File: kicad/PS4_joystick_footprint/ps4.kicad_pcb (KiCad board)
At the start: 2 copper layers, 20 x 28.5 mm, 2 parts, among them J1 Joystick, U1 COM-09032

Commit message: update pcb and documentation
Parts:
- added SW1: SW_Push, Button_Switch_SMD:SW_SPST_B3S-1000, F.Cu at (119.5, 140.5)
- added SW2: SW_Push, Button_Switch_SMD:SW_SPST_B3S-1000, F.Cu at (130.0, 151.0)
- added SW3: SW_Push, Button_Switch_SMD:SW_SPST_B3S-1000, F.Cu at (140.5, 140.5)
- added SW4: SW_Push, Button_Switch_SMD:SW_SPST_B3S-1000, F.Cu at (130.0, 130.0)
- J1: value Joystick -> Conn_01x11_Pin; footprint Connector_PinHeader_2.54mm:PinHeader_1x07_P2.54mm_Vertical -> Connector_PinHeader_2.54mm:PinHeader_1x11_P2.54mm_Vertical
- moved J1 23.9 mm to (91.9, 153.0), turned to 180 degrees
- moved U1 3.33 mm to (104.6, 144.0)
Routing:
- net /L2: track 0.00 -> 78.9 mm
- net /R2: track 0.00 -> 64.1 mm
- net /L1: track 0.00 -> 63.2 mm
- net /R1: track 0.00 -> 61.7 mm
- net /Switch: track 6.15 -> 18.4 mm
- net /R_black: track 17.3 -> 9.50 mm
- net /R_orange: track 24.4 -> 18.5 mm
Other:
- board size 20 x 28.5 mm -> 55.5 x 30 mm

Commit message: update joystick pcb
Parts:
- SW1: value SW_Push -> X
- SW2: value SW_Push -> A
- SW3: value SW_Push -> B
- SW4: value SW_Push -> Y
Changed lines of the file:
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@@
 		(tags "Tactile Switch")
 		(property "Reference" "SW4"
-			(at 0 4.3 180)
+			(at 0 0 180)
 			(layer "F.SilkS")
 			(effects
@@
 			)
 		)
-		(property "Value" "SW_Push"
+		(property "Value" "Y"
 			(at 0 4.5 0)
-			(layer "F.Fab")
-			(effects
-				(font
-					(size 1 1)
+			(layer "F.SilkS")
+			(effects
+				(font
+					(size 1.5 1.5)
 					(thickness 0.15)
 				)
@@
 		(tags "Tactile Switch")
 		(property "Reference" "SW1"
-			(at 0 5.1 180)
+			(at 0 0.04 180)
 			(layer "F.SilkS")
 			(effects
@@
 			)
 		)
-		(property "Value" "SW_Push"
-			(at 0 4.5 90)
-			(layer "F.Fab")
-			(effects
-				(font
-					(size 1 1)
+		(property "Value" "X"
+			(at 0 4.5 180)
+			(layer "F.SilkS")
+			(effects
+				(font
+					(size 1.5 1.5)
 					(thickness 0.15)
 				)
@@
 		(tags "Tactile Switch")
 		(property "Reference" "SW3"
-			(at 0 5.1 0)
+			(at -0.1 0 0)
 			(layer "F.SilkS")
 			(effects
@@
 			)
 		)
-		(property "Value" "SW_Push"
-			(at 0 4.5 90)
-			(layer "F.Fab")
-			(effects
-				(font
-					(size 1 1)
+		(property "Value" "B"
+			(at 0 4.5 180)
+			(layer "F.SilkS")
+			(effects
+				(font
+					(size 1.5 1.5)
 					(thickness 0.15)
 				)
@@
 		(tags "Tactile Switch")
 		(property "Reference" "SW2"
-			(at 0 -4.2 0)
+			(at 0 0 0)
 			(layer "F.SilkS")
 			(effects
@@
 			)
 		)
-		(property "Value" "SW_Push"
-			(at 0 4.5 0)
-			(layer "F.Fab")
-			(effects
-				(font
-					(size 1 1)
+		(property "Value" "A"
+			(at 0 -4.5 0)
+			(layer "F.SilkS")
+			(effects
+				(font
+					(size 1.5 1.5)
 					(thickness 0.15)
 				)
@@
 		)
 		(fp_text user "${REFERENCE}"
-			(at 0 -4.5 0)
-			(layer "F.Fab")
-			(effects
+			(at 0 4.5 0)
+			(layer "F.Fab")
+			(effects

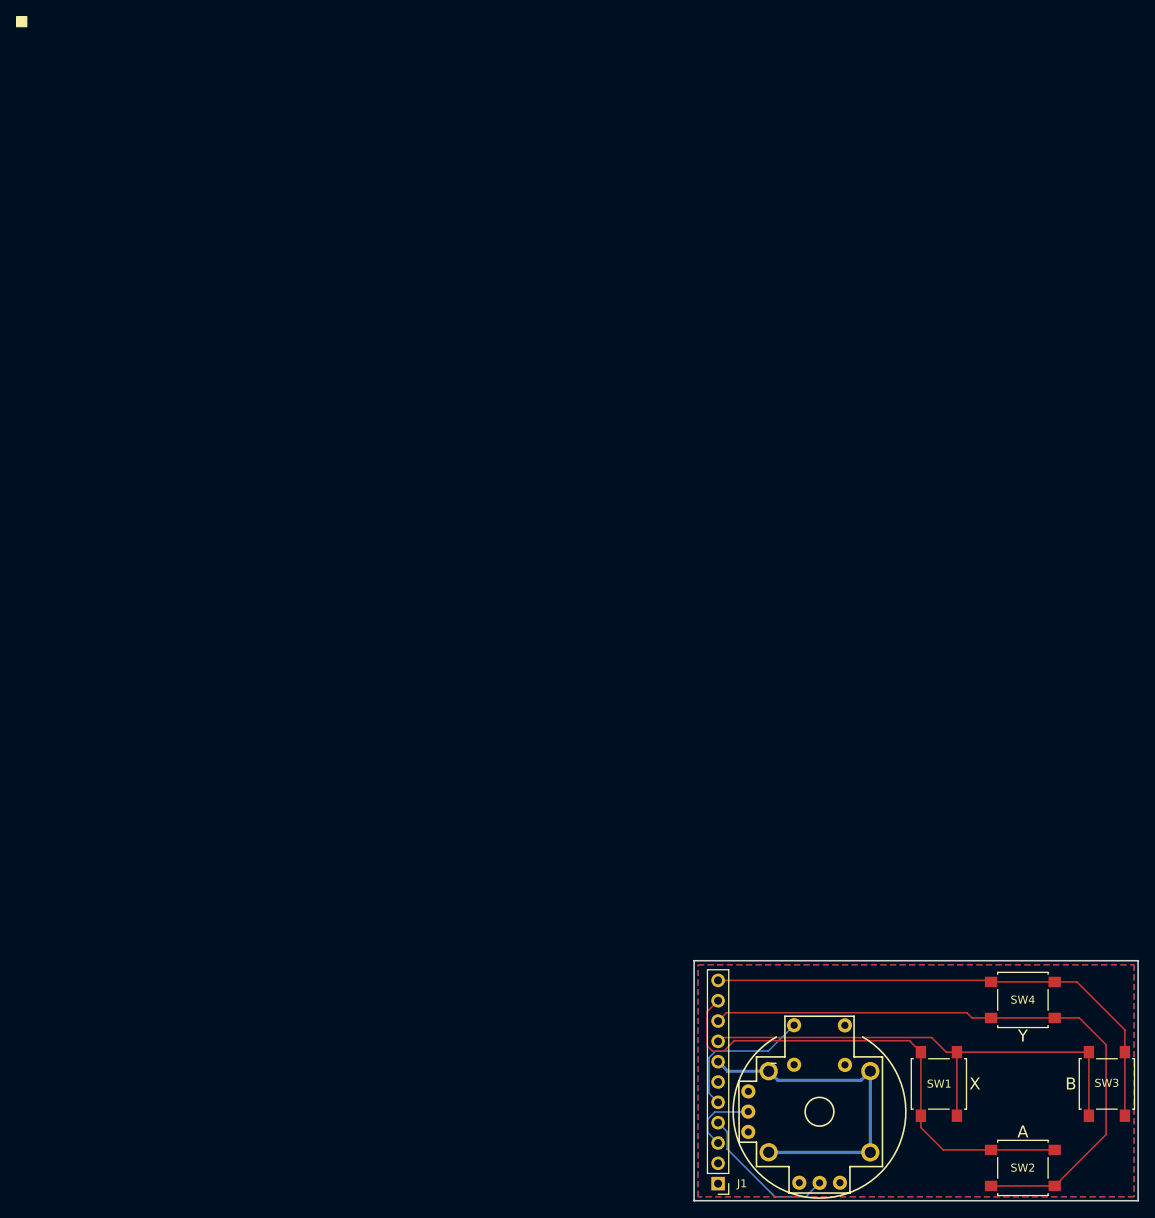
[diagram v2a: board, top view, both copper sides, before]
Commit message: add little-scale/PS4_joystick_footprint next to the footprint
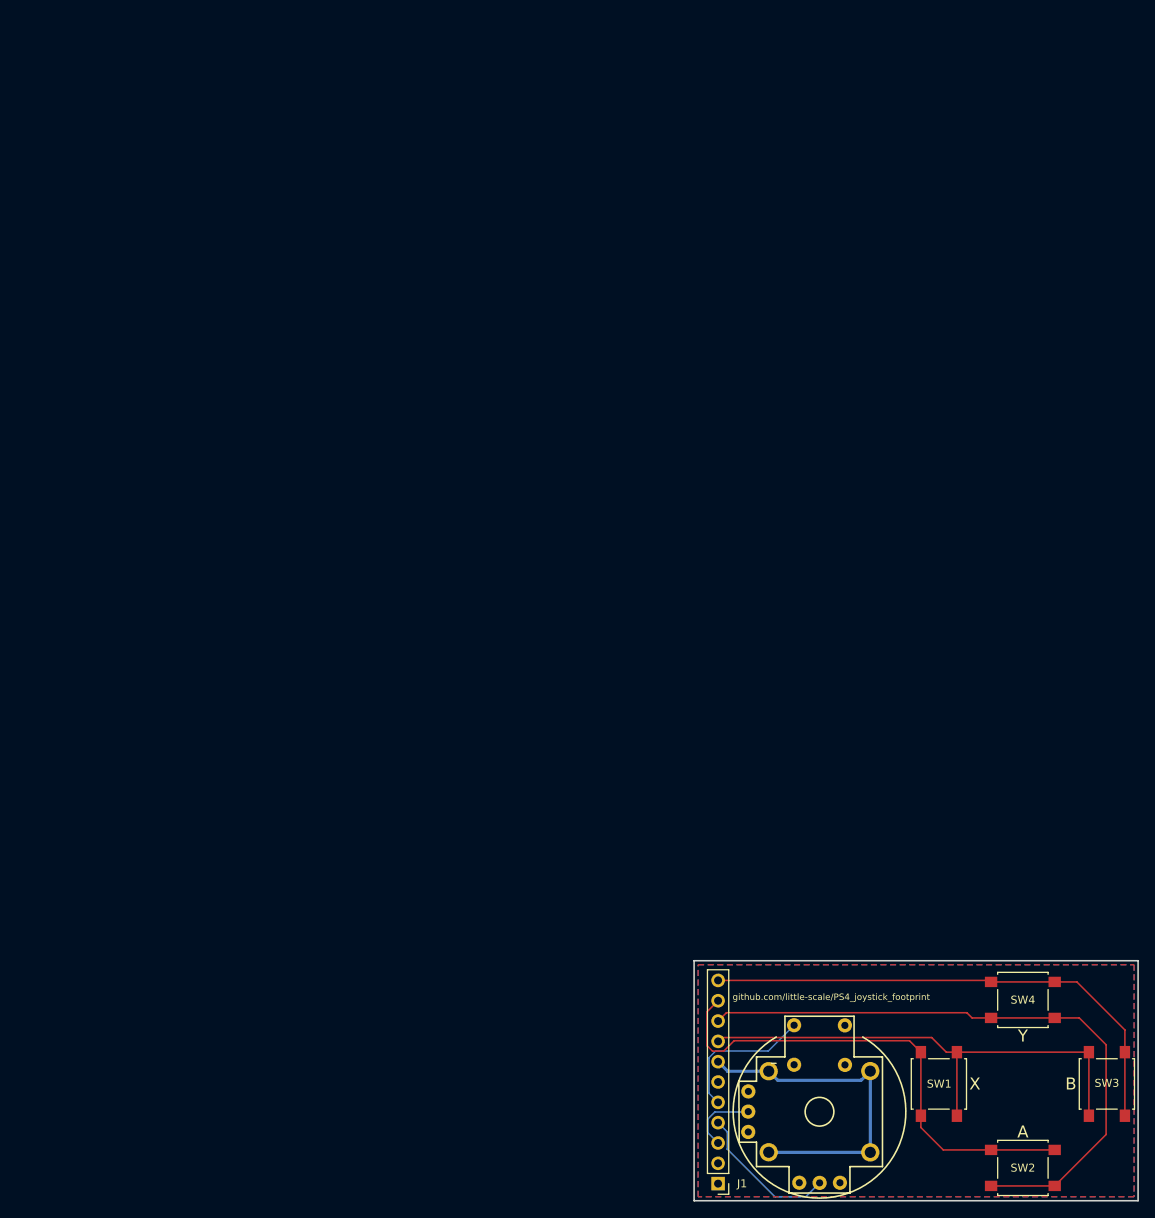
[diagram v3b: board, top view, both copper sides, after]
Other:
- board text added: "github.com/little-scale/PS4_joystick_footprint"
- board text removed: "JCLJLCJLCJLC"
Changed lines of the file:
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@@
-	)
-	(gr_rect
-		(start 4.213019 7.08255)
-		(end 5.483019 8.34255)
-		(stroke
-			(width 0.15)
-			(type solid)
-		)
-		(fill solid)
-		(layer "F.SilkS")
 	)
 	(gr_rect
@@
 		(layer "Edge.Cuts")
 	)
-	(gr_text "JCLJLCJLCJLC"
-		(at 15.875 17.78 0)
-		(layer "B.SilkS")
+	(gr_text "github.com/little-scale/PS4_joystick_footprint"
+		(at 93.7 130.1 0)
+		(layer "F.SilkS")
 		(effects
 			(font
-				(size 1.5 1.5)
-				(thickness 0.3)
+				(size 0.8 0.8)
+				(thickness 0.15)
 			)
-			(justify mirror)
+			(justify left bottom)
 		)
 	)
